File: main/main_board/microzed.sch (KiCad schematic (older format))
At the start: 16 parts, among them M1 microzed, U6 AP7361C-25SP-13, X1 microzed

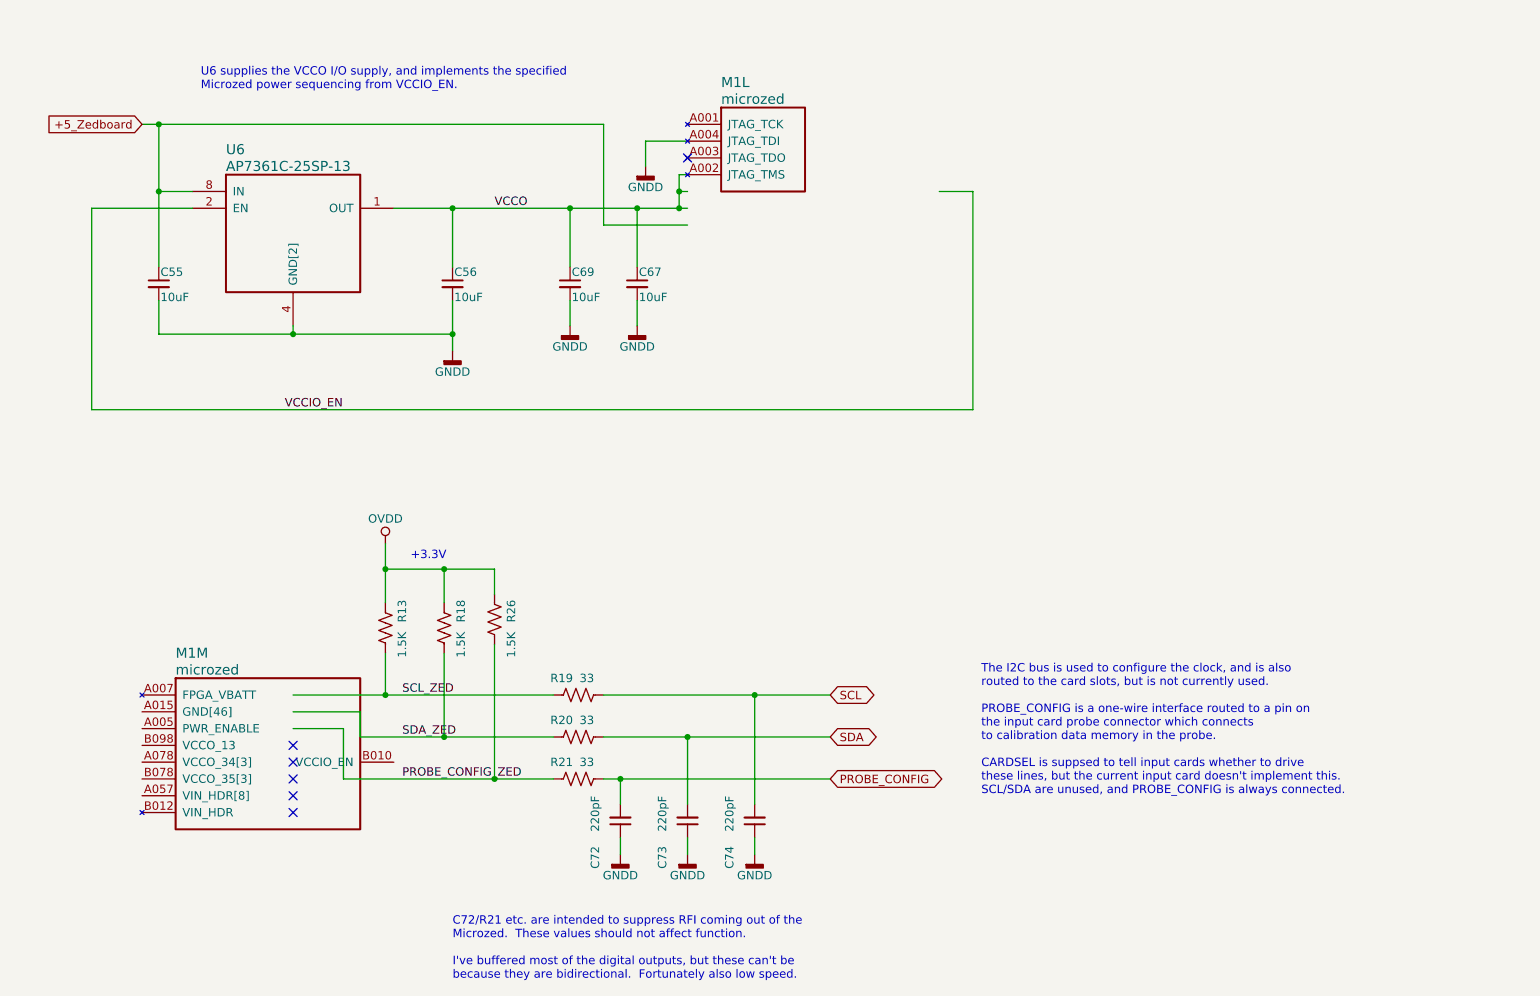
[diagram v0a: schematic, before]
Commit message: Added testpoints, debug IO port, LEDs, and clock output jack.
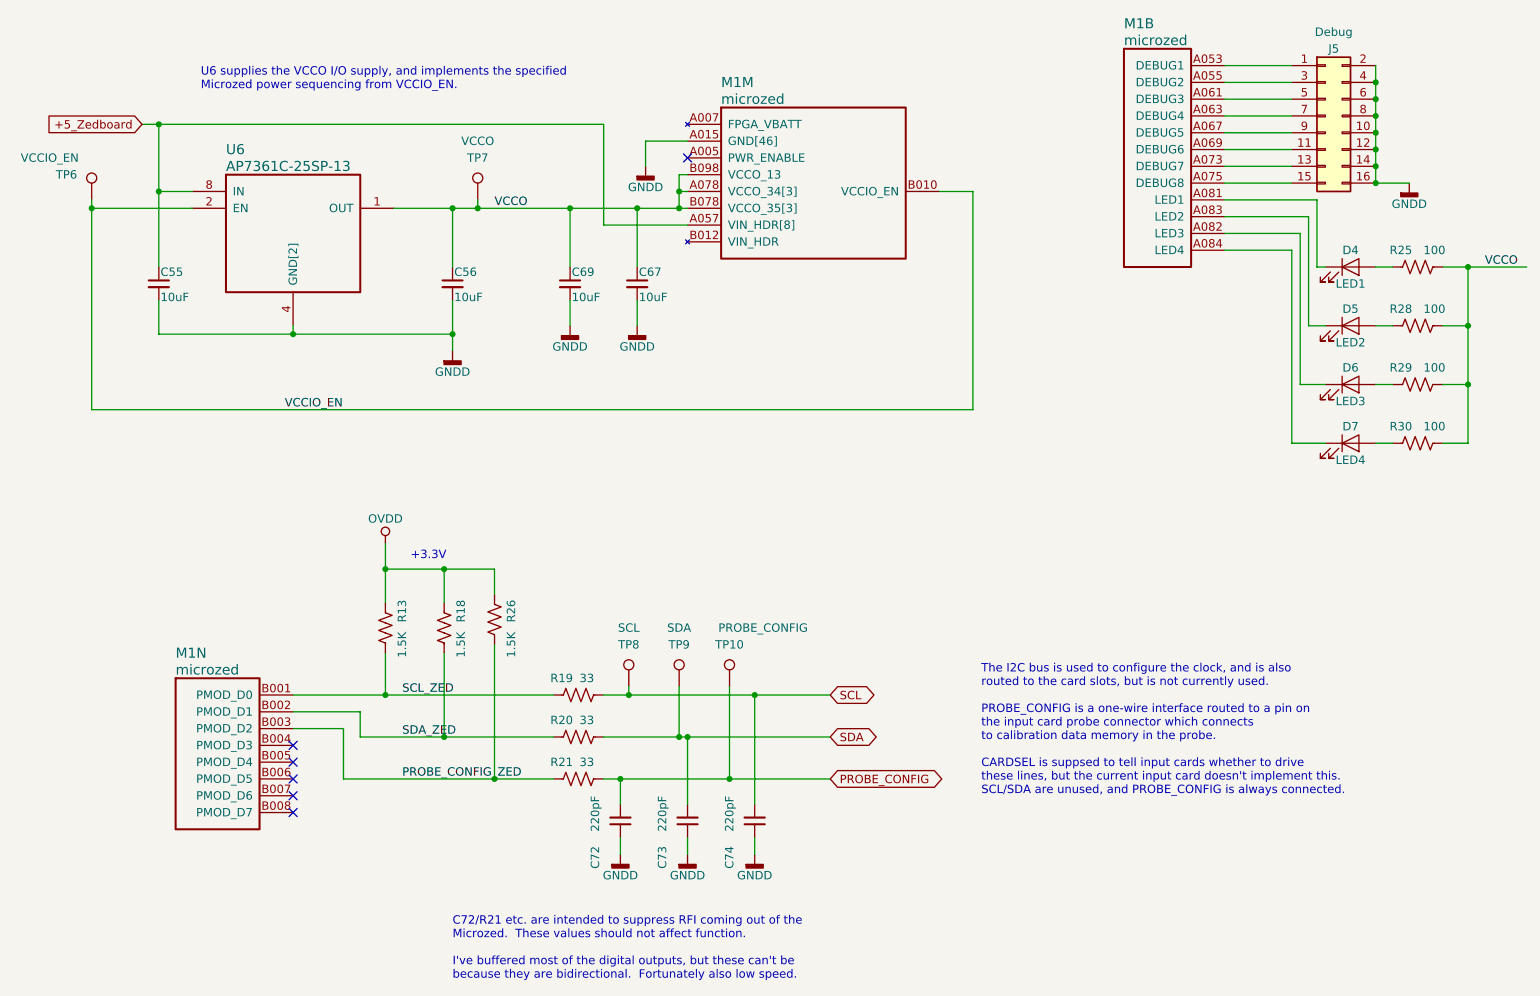
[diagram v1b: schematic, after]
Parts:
- added D4: LED1, LED_SMD:LED_0603_1608Metric_Castellated, symbol Device:LED
- added D5: LED2, LED_SMD:LED_0603_1608Metric_Castellated, symbol Device:LED
- added D6: LED3, LED_SMD:LED_0603_1608Metric_Castellated, symbol Device:LED
- added D7: LED4, LED_SMD:LED_0603_1608Metric_Castellated, symbol Device:LED
- added J5: Debug, Connector_PinHeader_2.54mm:PinHeader_2x08_P2.54mm_Vertical, symbol Connector_Generic:Conn_02x08_Odd_Even
- added unit 2 of M1
- added R25, R28, R29, R30: 100, Resistor_SMD:R_0603_1608Metric, symbol Device:R_US
- added TP10: PROBE_CONFIG, TestPoint:TestPoint_Keystone_5000-5004_Miniature, symbol Connector:TestPoint
- added TP6: VCCIO_EN, TestPoint:TestPoint_Keystone_5000-5004_Miniature, symbol Connector:TestPoint
- added TP7: VCCO, TestPoint:TestPoint_Keystone_5000-5004_Miniature, symbol Connector:TestPoint
- added TP8: SCL, TestPoint:TestPoint_Keystone_5000-5004_Miniature, symbol Connector:TestPoint
- added TP9: SDA, TestPoint:TestPoint_Keystone_5000-5004_Miniature, symbol Connector:TestPoint
- U6: DK line 24 -> 7
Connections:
- wire segments 65 -> 114

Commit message: Finishing up main/main_board/main_board.kicad_pcb.  Test points, stiching vias, ground pours.
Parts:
- J5: DK line (none) -> 38; Description (none) -> Connector Header Through Hole 16 position 0.100\" (2.54mm); Digikey (none) -> SAM10854-ND; MPN (none) -> TSW-108-07-F-D; Manufacturer (none) -> Samtec Inc.
- R13, R18, R26: Digikey RNCP0603FTD1K50CT-ND -> RMCF0603FT33R0CT-ND; MPN RNCP0603FTD1K50 -> RMCF0603FT33R0
- R19, R20, R21: Description RES 33.2 OHM 1% 1/8W 0603 -> RES 33 OHM 1% 1/10W 0603
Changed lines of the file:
@@
 F 1 "33" V 4600 5300 50  0000 C CNN
 F 2 "Resistor_SMD:R_0603_1608Metric" V 4740 5240 50  0001 C CNN
-F 3 "https://www.seielect.com/catalog/sei-rncp.pdf" H 4700 5250 50  0001 C CNN
-F 4 "RES 33.2 OHM 1% 1/8W 0603" H 4700 5250 50  0001 C CNN "Description"
+F 3 "https://www.seielect.com/catalog/sei-rmcf_rmcp.pdf" H 4700 5250 50  0001 C CNN
+F 4 "RES 33 OHM 1% 1/10W 0603" H 4700 5250 50  0001 C CNN "Description"
 F 5 "RNCP0603FTD33R2CT-ND" H 4700 5250 50  0001 C CNN "Digikey"
 F 6 "RNCP0603FTD33R2" H 4700 5250 50  0001 C CNN "MPN"
@@
 F 1 "33" V 4600 5550 50  0000 C CNN
 F 2 "Resistor_SMD:R_0603_1608Metric" V 4740 5490 50  0001 C CNN
-F 3 "https://www.seielect.com/catalog/sei-rncp.pdf" H 4700 5500 50  0001 C CNN
-F 4 "RES 33.2 OHM 1% 1/8W 0603" H 4700 5500 50  0001 C CNN "Description"
+F 3 "https://www.seielect.com/catalog/sei-rmcf_rmcp.pdf" H 4700 5500 50  0001 C CNN
+F 4 "RES 33 OHM 1% 1/10W 0603" H 4700 5500 50  0001 C CNN "Description"
 F 5 "RNCP0603FTD33R2CT-ND" H 4700 5500 50  0001 C CNN "Digikey"
 F 6 "RNCP0603FTD33R2" H 4700 5500 50  0001 C CNN "MPN"
@@
 F 1 "33" V 4600 5800 50  0000 C CNN
 F 2 "Resistor_SMD:R_0603_1608Metric" V 4740 5740 50  0001 C CNN
-F 3 "https://www.seielect.com/catalog/sei-rncp.pdf" H 4700 5750 50  0001 C CNN
-F 4 "RES 33.2 OHM 1% 1/8W 0603" H 4700 5750 50  0001 C CNN "Description"
+F 3 "https://www.seielect.com/catalog/sei-rmcf_rmcp.pdf" H 4700 5750 50  0001 C CNN
+F 4 "RES 33 OHM 1% 1/10W 0603" H 4700 5750 50  0001 C CNN "Description"
 F 5 "RNCP0603FTD33R2CT-ND" H 4700 5750 50  0001 C CNN "Digikey"
 F 6 "RNCP0603FTD33R2" H 4700 5750 50  0001 C CNN "MPN"
@@
 F 3 "https://www.seielect.com/catalog/sei-rncp.pdf" H 3550 4850 50  0001 C CNN
 F 4 "RES 1.5K OHM 1% 1/8W 0603" H 3550 4850 50  0001 C CNN "Description"
-F 5 "RNCP0603FTD1K50CT-ND" H 3550 4850 50  0001 C CNN "Digikey"
-F 6 "RNCP0603FTD1K50" H 3550 4850 50  0001 C CNN "MPN"
+F 5 "RMCF0603FT33R0CT-ND" H 3550 4850 50  0001 C CNN "Digikey"
+F 6 "RMCF0603FT33R0" H 3550 4850 50  0001 C CNN "MPN"
 F 7 "Stackpole Electronics Inc" H 3550 4850 50  0001 C CNN "Manufacturer"
 F 8 "32" H 3550 4850 50  0001 C CNN "DK line"
@@
 F 3 "https://www.seielect.com/catalog/sei-rncp.pdf" H 3900 4850 50  0001 C CNN
 F 4 "RES 1.5K OHM 1% 1/8W 0603" H 3900 4850 50  0001 C CNN "Description"
-F 5 "RNCP0603FTD1K50CT-ND" H 3900 4850 50  0001 C CNN "Digikey"
-F 6 "RNCP0603FTD1K50" H 3900 4850 50  0001 C CNN "MPN"
+F 5 "RMCF0603FT33R0CT-ND" H 3900 4850 50  0001 C CNN "Digikey"
+F 6 "RMCF0603FT33R0" H 3900 4850 50  0001 C CNN "MPN"
 F 7 "Stackpole Electronics Inc" H 3900 4850 50  0001 C CNN "Manufacturer"
 F 8 "32" H 3900 4850 50  0001 C CNN "DK line"
@@
 F 3 "https://www.seielect.com/catalog/sei-rncp.pdf" H 4200 4800 50  0001 C CNN
 F 4 "RES 1.5K OHM 1% 1/8W 0603" H 4200 4800 50  0001 C CNN "Description"
-F 5 "RNCP0603FTD1K50CT-ND" H 4200 4800 50  0001 C CNN "Digikey"
-F 6 "RNCP0603FTD1K50" H 4200 4800 50  0001 C CNN "MPN"
+F 5 "RMCF0603FT33R0CT-ND" H 4200 4800 50  0001 C CNN "Digikey"
+F 6 "RMCF0603FT33R0" H 4200 4800 50  0001 C CNN "MPN"
 F 7 "Stackpole Electronics Inc" H 4200 4800 50  0001 C CNN "Manufacturer"
 F 8 "32" H 4200 4800 50  0001 C CNN "DK line"
@@
 F 1 "Debug" H 9200 2300 50  0000 C CNN
 F 2 "Connector_PinHeader_2.54mm:PinHeader_2x08_P2.54mm_Vertical" H 9150 1800 50  0001 C CNN
-F 3 "~" H 9150 1800 50  0001 C CNN
+F 3 "http://suddendocs.samtec.com/catalog_english/tsw_th.pdf" H 9150 1800 50  0001 C CNN
+F 4 "38" H 9150 1800 50  0001 C CNN "DK line"
+F 5 "Connector Header Through Hole 16 position 0.100\" (2.54mm)" H 9150 1800 50  0001 C CNN "Description"
+F 6 "SAM10854-ND" H 9150 1800 50  0001 C CNN "Digikey"
+F 7 "TSW-108-07-F-D" H 9150 1800 50  0001 C CNN "MPN"
+F 8 "Samtec Inc." H 9150 1800 50  0001 C CNN "Manufacturer"
 	1    9150 1800
 	1    0    0    -1

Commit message: Main board seems to be about ready to be set off. Added gerber files. Made new footprints for the LEDs and DAC, since nothing in the standard footprints was a good match for the manufacturer recommended pattern. Moved around component values on the fab layer. Tweaked ground plane thermal via and fill width so that we get continuity between pins on the PCIe connectors. Moved OVDD vias to also avoid ground plane slotting. Added local copper pours on planes on U6 thermal pad to prevent thermal reliefs on the thermal vias.
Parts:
- D4, D5, D6, D7: footprint LED_SMD:LED_0603_1608Metric_Castellated -> main_board:WURTH_WL_SCMD_0603_LED
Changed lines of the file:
@@
 F 0 "D4" H 9300 2800 50  0000 C CNN
 F 1 "LED1" H 9300 2600 50  0000 C CNN
-F 2 "LED_SMD:LED_0603_1608Metric_Castellated" H 9300 2700 50  0001 C CNN
+F 2 "main_board:WURTH_WL_SCMD_0603_LED" H 9300 2700 50  0001 C CNN
 F 3 "https://katalog.we-online.de/pbs/datasheet/150060VS55040.pdf" H 9300 2700 50  0001 C CNN
 F 4 "37" H 9300 2700 50  0001 C CNN "DK line"
@@
 F 0 "D5" H 9300 3150 50  0000 C CNN
 F 1 "LED2" H 9300 2950 50  0000 C CNN
-F 2 "LED_SMD:LED_0603_1608Metric_Castellated" H 9300 3050 50  0001 C CNN
+F 2 "main_board:WURTH_WL_SCMD_0603_LED" H 9300 3050 50  0001 C CNN
 F 3 "https://katalog.we-online.de/pbs/datasheet/150060VS55040.pdf" H 9300 3050 50  0001 C CNN
 F 4 "37" H 9300 3050 50  0001 C CNN "DK line"
@@
 F 0 "D6" H 9300 3500 50  0000 C CNN
 F 1 "LED3" H 9300 3300 50  0000 C CNN
-F 2 "LED_SMD:LED_0603_1608Metric_Castellated" H 9300 3400 50  0001 C CNN
+F 2 "main_board:WURTH_WL_SCMD_0603_LED" H 9300 3400 50  0001 C CNN
 F 3 "https://katalog.we-online.de/pbs/datasheet/150060VS55040.pdf" H 9300 3400 50  0001 C CNN
 F 4 "37" H 9300 3400 50  0001 C CNN "DK line"
@@
 F 0 "D7" H 9300 3850 50  0000 C CNN
 F 1 "LED4" H 9300 3650 50  0000 C CNN
-F 2 "LED_SMD:LED_0603_1608Metric_Castellated" H 9300 3750 50  0001 C CNN
+F 2 "main_board:WURTH_WL_SCMD_0603_LED" H 9300 3750 50  0001 C CNN
 F 3 "https://katalog.we-online.de/pbs/datasheet/150060VS55040.pdf" H 9300 3750 50  0001 C CNN
 F 4 "37" H 9300 3750 50  0001 C CNN "DK line"
